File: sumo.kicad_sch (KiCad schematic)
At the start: 51 parts, among them Q1 BPW40, Q2 BPW40, SW1 SW_Push, SW2 SW_DIP_x01, T1 Screw_Terminal_01x04, T2 Screw_Terminal_01x04, T3 Screw_Terminal_01x04, T4 Screw_Terminal_01x04, T5 Screw_Terminal_01x04, U1 PIC16F628A-IP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

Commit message: motor driver
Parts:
- BT1, BT2, BT3: footprint (none) -> Battery:Battery_Pads
- C1: footprint Button_Switch_THT:SW_PUSH_1P1T_6x3.5mm_H5.0_APEM_MJTP1250 -> Capacitor_THT:C_Radial_D10.0mm_H12.5mm_P5.00mm
- SW2: footprint Button_Switch_SMD:SW_DIP_SPSTx01_Slide_9.78x4.72mm_W8.61mm_P2.54mm -> Button_Switch_THT:SW_DIP_SPSTx01_Slide_9.78x4.72mm_W7.62mm_P2.54mm
- T1, T2, T3, T4, T5: footprint TerminalBlock:TerminalBlock_bornier-4_P5.08mm -> TerminalBlock_MetzConnect:TerminalBlock_MetzConnect_Type086_RT03404HBLC_1x04_P3.81mm_Horizontal
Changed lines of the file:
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@@
 	(wire
 		(pts
-			(xy 39.37 138.43) (xy 39.37 134.62)
-		)
-		(stroke
-			(width 0)
-			(type default)
-		)
-	)
-	(wire
-		(pts
 			(xy 186.69 40.64) (xy 196.85 40.64)
 		)
@@
 			)
 		)
-		(property "Footprint" "TerminalBlock:TerminalBlock_bornier-4_P5.08mm"
+		(property "Footprint" "TerminalBlock_MetzConnect:TerminalBlock_MetzConnect_Type086_RT03404HBLC_1x04_P3.81mm_Horizontal"
 			(at 63.5 172.72 0)
 			(effects
@@
 			)
 		)
-		(property "Footprint" ""
+		(property "Footprint" "Battery:Battery_Pads"
 			(at 25.4 68.326 90)
 			(effects
@@
 			)
 		)
-		(property "Footprint" "TerminalBlock:TerminalBlock_bornier-4_P5.08mm"
+		(property "Footprint" "TerminalBlock_MetzConnect:TerminalBlock_MetzConnect_Type086_RT03404HBLC_1x04_P3.81mm_Horizontal"
 			(at 158.75 190.5 0)
 			(effects
@@
 			)
 		)
-		(property "Footprint" "Button_Switch_SMD:SW_DIP_SPSTx01_Slide_9.78x4.72mm_W8.61mm_P2.54mm"
+		(property "Footprint" "Button_Switch_THT:SW_DIP_SPSTx01_Slide_9.78x4.72mm_W7.62mm_P2.54mm"
 			(at 123.19 125.73 0)
 			(effects
@@
 			)
 		)
-		(property "Footprint" ""
+		(property "Footprint" "Battery:Battery_Pads"
 			(at 112.014 125.73 90)
 			(effects
@@
 			)
 		)
-		(property "Footprint" "Button_Switch_THT:SW_PUSH_1P1T_6x3.5mm_H5.0_APEM_MJTP1250"
+		(property "Footprint" "Capacitor_THT:C_Radial_D10.0mm_H12.5mm_P5.00mm"
 			(at 39.37 152.4 0)
 			(effects
@@
 			)
 		)
-		(property "Footprint" ""
+		(property "Footprint" "Battery:Battery_Pads"
 			(at 27.94 178.816 90)
 			(effects
@@
 			)
 		)
-		(property "Footprint" "TerminalBlock:TerminalBlock_bornier-4_P5.08mm"
+		(property "Footprint" "TerminalBlock_MetzConnect:TerminalBlock_MetzConnect_Type086_RT03404HBLC_1x04_P3.81mm_Horizontal"
 			(at 90.17 142.24 0)
 			(effects
@@
 			)
 		)
-		(property "Footprint" "TerminalBlock:TerminalBlock_bornier-4_P5.08mm"
+		(property "Footprint" "TerminalBlock_MetzConnect:TerminalBlock_MetzConnect_Type086_RT03404HBLC_1x04_P3.81mm_Horizontal"
 			(at 92.71 80.01 0)
 			(effects
@@
 			)
 		)
-		(property "Footprint" "TerminalBlock:TerminalBlock_bornier-4_P5.08mm"
+		(property "Footprint" "TerminalBlock_MetzConnect:TerminalBlock_MetzConnect_Type086_RT03404HBLC_1x04_P3.81mm_Horizontal"
 			(at 160.02 111.76 0)
 			(effects

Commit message: schematic updates
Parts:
- added D7, D8: IR LED, LED_THT:LED_D5.0mm_IRBlack, symbol LED:IR204A
- added SW3, SW4: SW_DIP_x01, Button_Switch_THT:SW_DIP_SPSTx01_Slide_9.78x4.72mm_W7.62mm_P2.54mm, symbol Switch:SW_DIP_x01
- D1, D2, D5, D6: footprint LED_THT:LED_D3.0mm -> LED_THT:LED_D5.0mm
- D3, D4: footprint LED_THT:LED_D3.0mm_IRBlack -> LED_THT:LED_D5.0mm_IRBlack
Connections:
- net +5V: now also SW3.1, SW4.1
- net +6V: now also C3.1
- net GNDREF: now also C3.2
- net at D3.1 (K), D4.1 (K), R8.1: now also D7.1 (K), D8.1 (K)
- net at R15.1: now also T5.3 (Pin_3); no longer T5.2 (Pin_2)
- net at R12.2: now also T5.1 (Pin_1); no longer T5.3 (Pin_3)
- net at U1.15 (CLKOUT/OSC2/RA6): now also SW4.2
- net at U1.16 (CLKIN/OSC1/RA7): now also SW3.2
- net at R6.1: now also T5.2 (Pin_2); no longer T5.1 (Pin_1)
- net at D3.2 (A), D4.2 (A), U4.6: now also D7.2 (A), D8.2 (A)
- no-connect marks 6 -> 8
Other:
- note added: "TODO: add switch(es)"
- moved on the sheet: BT2, C1, R1, SW1, T1, T2, U1, U2

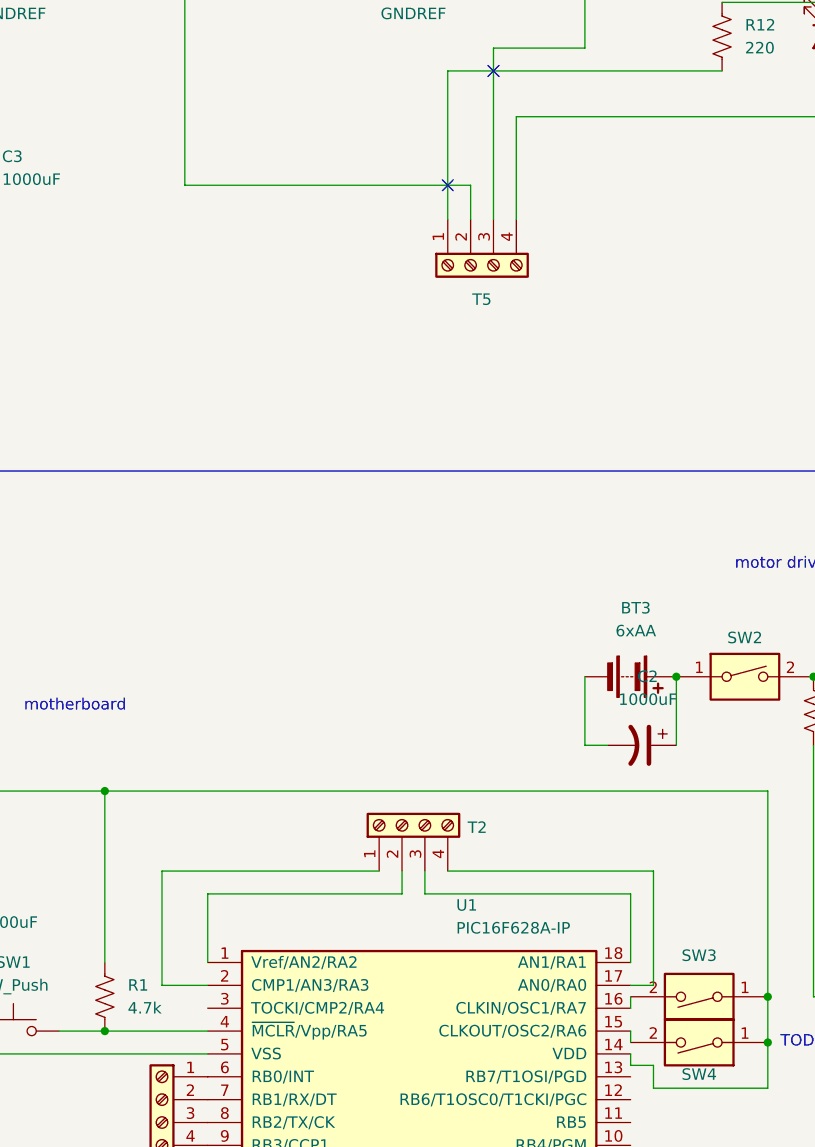
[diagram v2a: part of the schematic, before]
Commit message: connect grounds
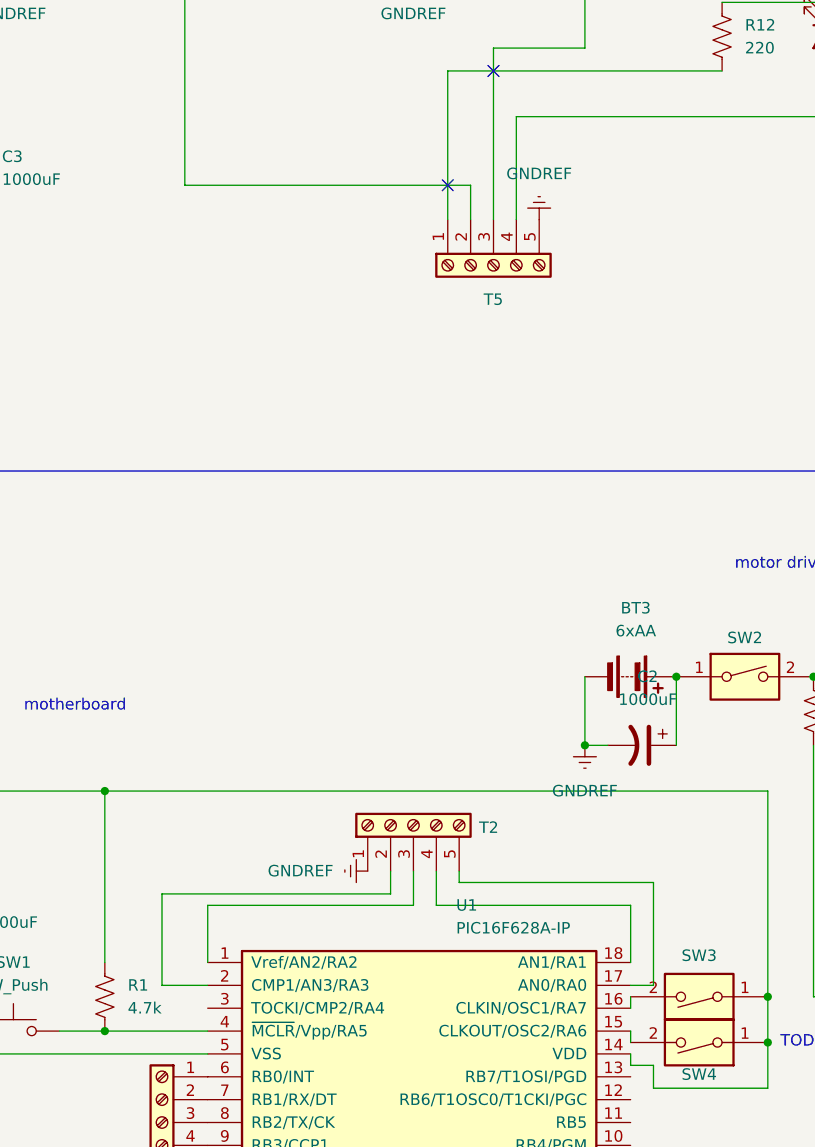
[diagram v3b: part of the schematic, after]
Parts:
- T2, T5: footprint TerminalBlock_MetzConnect:TerminalBlock_MetzConnect_Type086_RT03404HBLC_1x04_P3.81mm_Horizontal -> TerminalBlock_MetzConnect:TerminalBlock_MetzConnect_Type086_RT03405HBLC_1x05_P3.81mm_Horizontal; symbol Connector:Screw_Terminal_01x04 -> Connector:Screw_Terminal_01x05
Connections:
- net GNDREF: now also BT3.2 (-), C2.2, T2.1 (Pin_1), T5.5 (Pin_5)
- net at U1.1 (Vref/AN2/RA2): now also T2.3 (Pin_3); no longer T2.2 (Pin_2)
- net at U1.17 (AN0/RA0): now also T2.5 (Pin_5); no longer T2.4 (Pin_4)
- net at U1.18 (AN1/RA1): now also T2.4 (Pin_4); no longer T2.3 (Pin_3)
- net at U1.2 (CMP1/AN3/RA3): now also T2.2 (Pin_2); no longer T2.1 (Pin_1)

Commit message: sensors
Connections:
- net +6V: now also U4.13; no longer U4.12
- net at R8.2: now also U4.12; no longer U4.13
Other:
- moved on the sheet: U4F
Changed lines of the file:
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@@
 	(symbol
 		(lib_id "74xx:74HC04")
-		(at 267.97 83.82 270)
+		(at 267.97 83.82 90)
 		(unit 6)
 		(exclude_from_sim no)
@@
 		(dnp no)
 		(property "Reference" "U4"
-			(at 277.114 83.82 0)
+			(at 258.826 83.82 0)
 			(effects
 				(font
@@
 		)
 		(property "Value" "74HC04"
-			(at 274.32 83.82 0)
+			(at 261.62 83.82 0)
 			(effects
 				(font

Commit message: save changes
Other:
- note removed: "TODO: add switch(es)"
- note removed: "webb's schematic says 12->13??"
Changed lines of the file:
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@@
-		)
-	)
-	(text "webb's schematic says 12->13??\n"
-		(exclude_from_sim no)
-		(at 246.38 84.836 0)
-		(effects
-			(font
-				(size 1.27 1.27)
-			)
 		)
 	)
@@
 		(effects
 			(font
-				(size 1.27 1.27)
-			)
-		)
-	)
-	(text "TODO: add switch(es)"
-		(exclude_from_sim no)
-		(at 136.652 166.37 0)
-		(effects
-			(font

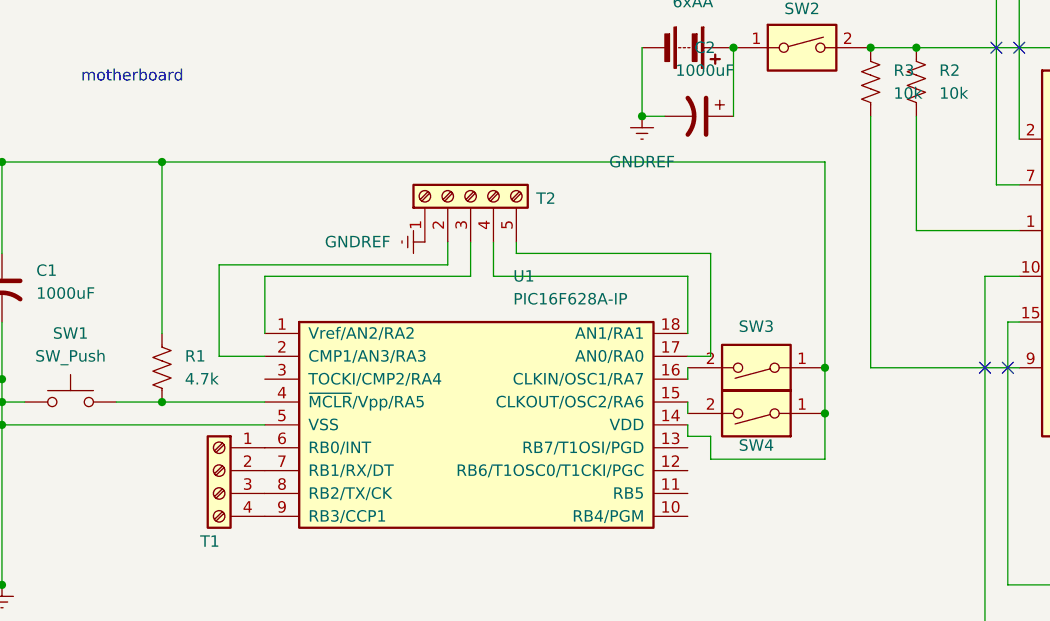
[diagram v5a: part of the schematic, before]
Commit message: change potentiometer footprint
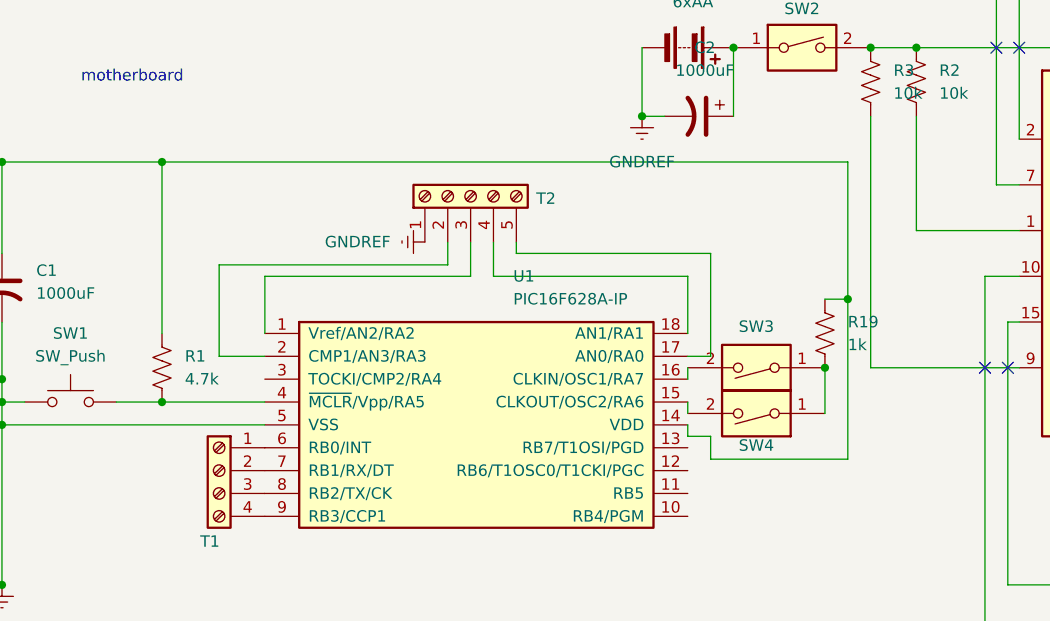
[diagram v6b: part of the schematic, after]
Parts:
- added R19: 1k, Resistor_THT:R_Axial_DIN0207_L6.3mm_D2.5mm_P7.62mm_Horizontal, symbol Device:R_US
- VR1: footprint Potentiometer_THT:Potentiometer_Bourns_3386F_Vertical -> Potentiometer_THT:Potentiometer_Bourns_3386P_Vertical
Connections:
- net +5V: now also R19.1; no longer SW3.1, SW4.1
- new net: R19.2, SW3.1, SW4.1
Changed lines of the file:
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@@
-	)
-	(junction
-		(at 125.73 166.37)
-		(diameter 0)
-		(color 0 0 0 0)
 	)
 	(junction
@@
 	)
 	(junction
+		(at 128.27 153.67)
+		(diameter 0)
+		(color 0 0 0 0)
+	)
+	(junction
 		(at 52.07 138.43)
 		(diameter 0)
@@
 	)
 	(junction
+		(at 125.73 161.29)
+		(diameter 0)
+		(color 0 0 0 0)
+	)
+	(junction
 		(at 267.97 93.98)
 		(diameter 0)
@@
 	(junction
 		(at 149.86 40.64)
-		(diameter 0)
-		(color 0 0 0 0)
-	)
-	(junction
-		(at 125.73 161.29)
 		(diameter 0)
 		(color 0 0 0 0)
@@
 	(wire
 		(pts
+			(xy 113.03 171.45) (xy 128.27 171.45)
+		)
+		(stroke
+			(width 0)
+			(type default)
+		)
+	)
+	(wire
+		(pts
 			(xy 158.75 181.61) (xy 158.75 185.42)
 		)
@@
 	(wire
 		(pts
+			(xy 128.27 153.67) (xy 128.27 171.45)
+		)
+		(stroke
+			(width 0)
+			(type default)
+		)
+	)
+	(wire
+		(pts
 			(xy 24.13 30.48) (xy 24.13 36.83)
 		)
@@
 	(wire
 		(pts
-			(xy 125.73 166.37) (xy 125.73 171.45)
-		)
-		(stroke
-			(width 0)
-			(type default)
-		)
-	)
-	(wire
-		(pts
 			(xy 172.72 151.13) (xy 175.26 151.13)
 		)
@@
 	(wire
 		(pts
-			(xy 125.73 161.29) (xy 125.73 138.43)
+			(xy 125.73 161.29) (xy 125.73 166.37)
+		)
+		(stroke
+			(width 0)
+			(type default)
+		)
+	)
+	(wire
+		(pts
+			(xy 128.27 138.43) (xy 128.27 153.67)
 		)
 		(stroke
@@
 	(wire
 		(pts
+			(xy 52.07 138.43) (xy 128.27 138.43)
+		)
+		(stroke
+			(width 0)
+			(type default)
+		)
+	)
+	(wire
+		(pts
 			(xy 255.27 26.67) (xy 267.97 26.67)
 		)
@@
 	(wire
 		(pts
+			(xy 125.73 153.67) (xy 128.27 153.67)
+		)
+		(stroke
+			(width 0)
+			(type default)
+		)
+	)
+	(wire
+		(pts
 			(xy 110.49 161.29) (xy 110.49 162.56)
 		)
@@
 	(wire
 		(pts
-			(xy 125.73 161.29) (xy 125.73 166.37)
-		)
-		(stroke
-			(width 0)
-			(type default)
-		)
-	)
-	(wire
-		(pts
 			(xy 186.69 35.56) (xy 186.69 40.64)
 		)
@@
 	(wire
 		(pts
-			(xy 113.03 171.45) (xy 125.73 171.45)
-		)
-		(stroke
-			(width 0)
-			(type default)
-		)
-	)
-	(wire
-		(pts
 			(xy 86.36 30.48) (xy 86.36 33.02)
-		)
-		(stroke
-			(width 0)
-			(type default)
-		)
-	)
-	(wire
-		(pts
-			(xy 52.07 138.43) (xy 125.73 138.43)
 		)
 		(stroke
@@
 			)
 		)
-		(property "Footprint" "Potentiometer_THT:Potentiometer_Bourns_3386F_Vertical"
+		(property "Footprint" "Potentiometer_THT:Potentiometer_Bourns_3386P_Vertical"
 			(at 238.76 50.8 0)
 			(effects
@@
 					(unit 1)
 				)
+			)
+		)
+	)
+	(symbol
+		(lib_id "Device:R_US")
+		(at 125.73 157.48 0)
+		(unit 1)
+		(exclude_from_sim no)
+		(in_bom yes)
+		(on_board yes)
+		(dnp no)
+		(fields_autoplaced yes)
+		(property "Reference" "R19"
+			(at 128.27 156.2099 0)
+			(effects
+				(font
+					(size 1.27 1.27)
+				)
+				(justify left)
+			)
+		)
+		(property "Value" "1k"
+			(at 128.27 158.7499 0)
+			(effects
+				(font
+					(size 1.27 1.27)
+				)
+				(justify left)
+			)
+		)
+		(property "Footprint" "Resistor_THT:R_Axial_DIN0207_L6.3mm_D2.5mm_P7.62mm_Horizontal"
+			(at 126.746 157.734 90)
+			(effects
+				(font
+					(size 1.27 1.27)
+				)
+				(hide yes)
+			)
+		)
+		(property "Datasheet" "~"
+			(at 125.73 157.48 0)
+			(effects
+				(font
+					(size 1.27 1.27)
+				)
+				(hide yes)
+			)
+		)
+		(property "Description" "Resistor, US symbol"
+			(at 125.73 157.48 0)
+			(effects
+				(font
+					(size 1.27 1.27)
+				)
+				(hide yes)
+			)
+		)
+		(pin "2"
+		)
+		(pin "1"
+		)
+		(instances
+			(project "sumo"
+				(path "/b3326479-b174-4648-80e1-7cc32064c8ef"
+					(reference "R19")
+					(unit 1)
+				)

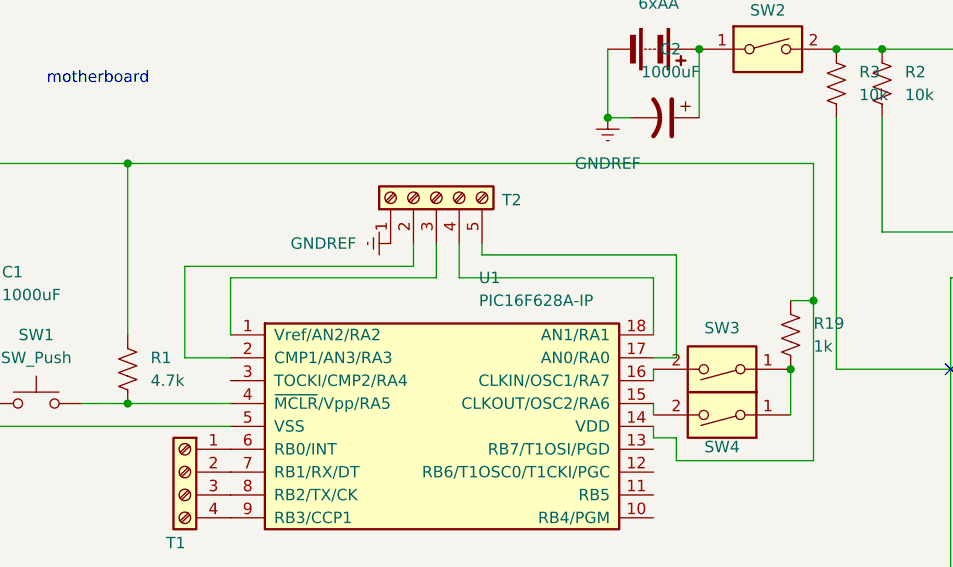
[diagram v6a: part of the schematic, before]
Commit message: remove ground plane
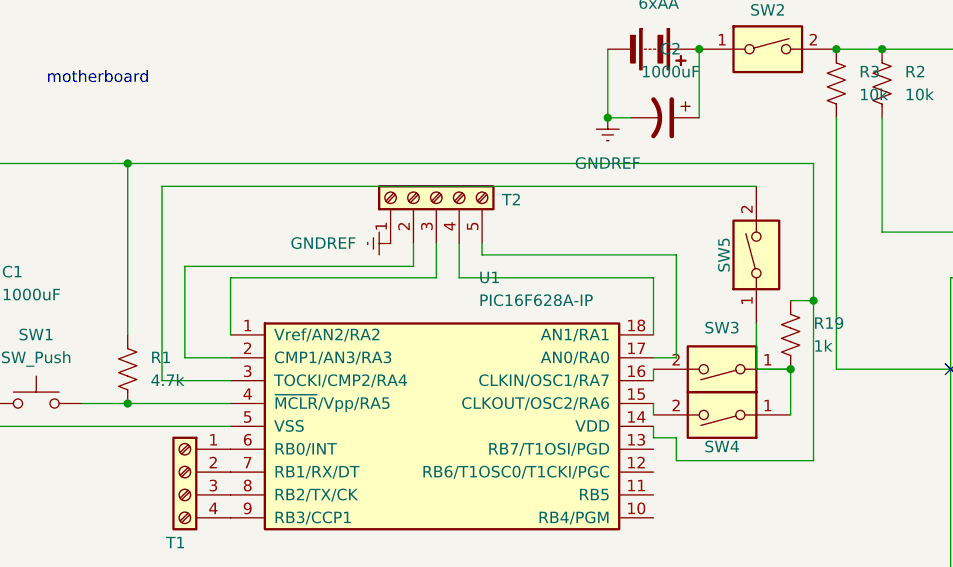
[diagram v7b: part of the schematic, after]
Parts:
- added SW5: SW_DIP_x01, Connector_Wire:SolderWire-0.1sqmm_1x02_P3.6mm_D0.4mm_OD1mm, symbol Switch:SW_DIP_x01
- T1, T3, T4: footprint TerminalBlock_MetzConnect:TerminalBlock_MetzConnect_Type086_RT03404HBLC_1x04_P3.81mm_Horizontal -> TerminalBlock_MetzConnect:TerminalBlock_MetzConnect_Type101_RT01604HBWC_1x04_P5.08mm_Horizontal
- T2, T5: value Screw_Terminal_01x04 -> Screw_Terminal_01x05; footprint TerminalBlock_MetzConnect:TerminalBlock_MetzConnect_Type086_RT03405HBLC_1x05_P3.81mm_Horizontal -> TerminalBlock_MetzConnect:TerminalBlock_MetzConnect_Type101_RT01605HBWC_1x05_P5.08mm_Horizontal
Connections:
- net at R19.2, SW3.1, SW4.1: now also SW5.1
- net at U1.3 (TOCKI/CMP2/RA4): now also SW5.2
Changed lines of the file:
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@@
 	(wire
 		(pts
+			(xy 55.88 140.97) (xy 55.88 162.56)
+		)
+		(stroke
+			(width 0)
+			(type default)
+		)
+	)
+	(wire
+		(pts
 			(xy 172.72 151.13) (xy 175.26 151.13)
 		)
@@
 	(wire
 		(pts
+			(xy 121.92 140.97) (xy 55.88 140.97)
+		)
+		(stroke
+			(width 0)
+			(type default)
+		)
+	)
+	(wire
+		(pts
 			(xy 234.95 50.8) (xy 234.95 41.91)
 		)
@@
 	(wire
 		(pts
+			(xy 125.73 161.29) (xy 121.92 161.29)
+		)
+		(stroke
+			(width 0)
+			(type default)
+		)
+	)
+	(wire
+		(pts
 			(xy 25.4 64.77) (xy 36.83 64.77)
 		)
@@
 	(wire
 		(pts
+			(xy 121.92 161.29) (xy 121.92 156.21)
+		)
+		(stroke
+			(width 0)
+			(type default)
+		)
+	)
+	(wire
+		(pts
 			(xy 92.71 71.12) (xy 92.71 74.93)
 		)
@@
 	(wire
 		(pts
+			(xy 55.88 162.56) (xy 63.5 162.56)
+		)
+		(stroke
+			(width 0)
+			(type default)
+		)
+	)
+	(wire
+		(pts
 			(xy 186.69 35.56) (xy 186.69 40.64)
 		)
@@
 			)
 		)
-		(property "Footprint" "TerminalBlock_MetzConnect:TerminalBlock_MetzConnect_Type086_RT03404HBLC_1x04_P3.81mm_Horizontal"
+		(property "Footprint" "TerminalBlock_MetzConnect:TerminalBlock_MetzConnect_Type101_RT01604HBWC_1x04_P5.08mm_Horizontal"
 			(at 58.42 172.72 0)
 			(effects
@@
 			)
 		)
-		(property "Footprint" "TerminalBlock_MetzConnect:TerminalBlock_MetzConnect_Type086_RT03404HBLC_1x04_P3.81mm_Horizontal"
+		(property "Footprint" "TerminalBlock_MetzConnect:TerminalBlock_MetzConnect_Type101_RT01604HBWC_1x04_P5.08mm_Horizontal"
 			(at 158.75 190.5 0)
 			(effects
@@
 			)
 		)
-		(property "Value" "Screw_Terminal_01x04"
+		(property "Value" "Screw_Terminal_01x05"
 			(at 88.8999 139.7 0)
 			(effects
@@
 			)
 		)
-		(property "Footprint" "TerminalBlock_MetzConnect:TerminalBlock_MetzConnect_Type086_RT03405HBLC_1x05_P3.81mm_Horizontal"
+		(property "Footprint" "TerminalBlock_MetzConnect:TerminalBlock_MetzConnect_Type101_RT01605HBWC_1x05_P5.08mm_Horizontal"
 			(at 86.36 142.24 0)
 			(effects
@@
 	)
 	(symbol
+		(lib_id "Switch:SW_DIP_x01")
+		(at 121.92 148.59 90)
+		(unit 1)
+		(exclude_from_sim no)
+		(in_bom yes)
+		(on_board yes)
+		(dnp no)
+		(property "Reference" "SW5"
+			(at 118.364 148.59 0)
+			(effects
+				(font
+					(size 1.27 1.27)
+				)
+			)
+		)
+		(property "Value" "SW_DIP_x01"
+			(at 127 148.59 0)
+			(effects
+				(font
+					(size 1.27 1.27)
+				)
+				(hide yes)
+			)
+		)
+		(property "Footprint" "Connector_Wire:SolderWire-0.1sqmm_1x02_P3.6mm_D0.4mm_OD1mm"
+			(at 121.92 148.59 0)
+			(effects
+				(font
+					(size 1.27 1.27)
+				)
+				(hide yes)
+			)
+		)
+		(property "Datasheet" "~"
+			(at 121.92 148.59 0)
+			(effects
+				(font
+					(size 1.27 1.27)
+				)
+				(hide yes)
+			)
+		)
+		(property "Description" "1x DIP Switch, Single Pole Single Throw (SPST) switch, small symbol"
+			(at 121.92 148.59 0)
+			(effects
+				(font
+					(size 1.27 1.27)
+				)
+				(hide yes)
+			)
+		)
+		(pin "1"
+		)
+		(pin "2"
+		)
+		(instances
+			(project "sumo"
+				(path "/b3326479-b174-4648-80e1-7cc32064c8ef"
+					(reference "SW5")
+					(unit 1)
+				)
+			)
+		)
+	)
+	(symbol
 		(lib_id "74xx:74HC04")
 		(at 267.97 49.53 270)
@@
 			)
 		)
-		(property "Value" "Screw_Terminal_01x04"
+		(property "Value" "Screw_Terminal_01x05"
 			(at 96.52 86.36 90)
 			(effects
@@
 			)
 		)
-		(property "Footprint" "TerminalBlock_MetzConnect:TerminalBlock_MetzConnect_Type086_RT03405HBLC_1x05_P3.81mm_Horizontal"
+		(property "Footprint" "TerminalBlock_MetzConnect:TerminalBlock_MetzConnect_Type101_RT01605HBWC_1x05_P5.08mm_Horizontal"
 			(at 95.25 80.01 0)
 			(effects
@@
 			)
 		)
-		(property "Footprint" "TerminalBlock_MetzConnect:TerminalBlock_MetzConnect_Type086_RT03404HBLC_1x04_P3.81mm_Horizontal"
+		(property "Footprint" "TerminalBlock_MetzConnect:TerminalBlock_MetzConnect_Type101_RT01604HBWC_1x04_P5.08mm_Horizontal"
 			(at 160.02 111.76 0)
 			(effects
